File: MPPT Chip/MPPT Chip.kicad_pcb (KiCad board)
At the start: 2 copper layers, 2 parts

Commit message: 11/10 meeting updates
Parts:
- removed REF**: MAX20801, MAX20801:MAX20801
- removed REF**: PinHeader, MAX20801:PinHeader
- added J1: Conn_02x05_Counter_Clockwise, MAX20801:PinHeader, B.Cu at (75.5, 98.3)
- added U0: MAX20801, MAX20801:MAX20801, F.Cu at (79.0, 96.5)
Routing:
- net (no net): track 132.3 -> 0.00 mm, vias 10 -> 0
- net GND: track 0.00 -> 37.9 mm, vias 0 -> 3
- net Net-(J1-Pad5): track 0.00 -> 30.1 mm, vias 0 -> 1
- net Net-(J1-Pad10): track 0.00 -> 26.4 mm, vias 0 -> 1
- net Net-(J1-Pad9): track 0.00 -> 22.1 mm, vias 0 -> 1
- net Net-(J1-Pad1): track 0.00 -> 20.9 mm, vias 0 -> 1
- net Net-(J1-Pad8): track 0.00 -> 17.5 mm, vias 0 -> 1
- net Net-(J1-Pad2): track 0.00 -> 16.3 mm, vias 0 -> 1
- net Net-(J1-Pad6): track 0.00 -> 5.34 mm, vias 0 -> 1
- added copper zone on B.Cu, net GND
- added copper zone on F.Cu, net GND
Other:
- board outline added: 30 x 15 mm

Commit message: gerber files
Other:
- board text added: "BSE MAX 20801"
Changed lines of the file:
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@@
   (general
     (thickness 1.6)
-    (drawings 4)
+    (drawings 5)
     (tracks 84)
     (zones 0)
@@
     (pcbplotparams
       (layerselection 0x010fc_ffffffff)
-      (usegerberextensions false)
+      (usegerberextensions true)
       (usegerberattributes true)
       (usegerberadvancedattributes true)
@@
       (psa4output false)
       (plotreference true)
-      (plotvalue true)
+      (plotvalue false)
       (plotinvisibletext false)
       (padsonsilk false)
@@
       (outputformat 1)
       (mirror false)
-      (drillshape 1)
+      (drillshape 0)
       (scaleselection 1)
-      (outputdirectory ""))
+      (outputdirectory "gerbers/"))
   )
   (net 0 "")
@@
       (net 6 "Net-(J1-Pad5)"))
   )
+  (gr_text "BSE MAX 20801" (at 83.5 103.5) (layer F.SilkS)
+    (effects (font (size 1 1) (thickness 0.15)))
+  )
   (gr_line (start 60 90) (end 60 105) (layer Edge.Cuts) (width 0.001))

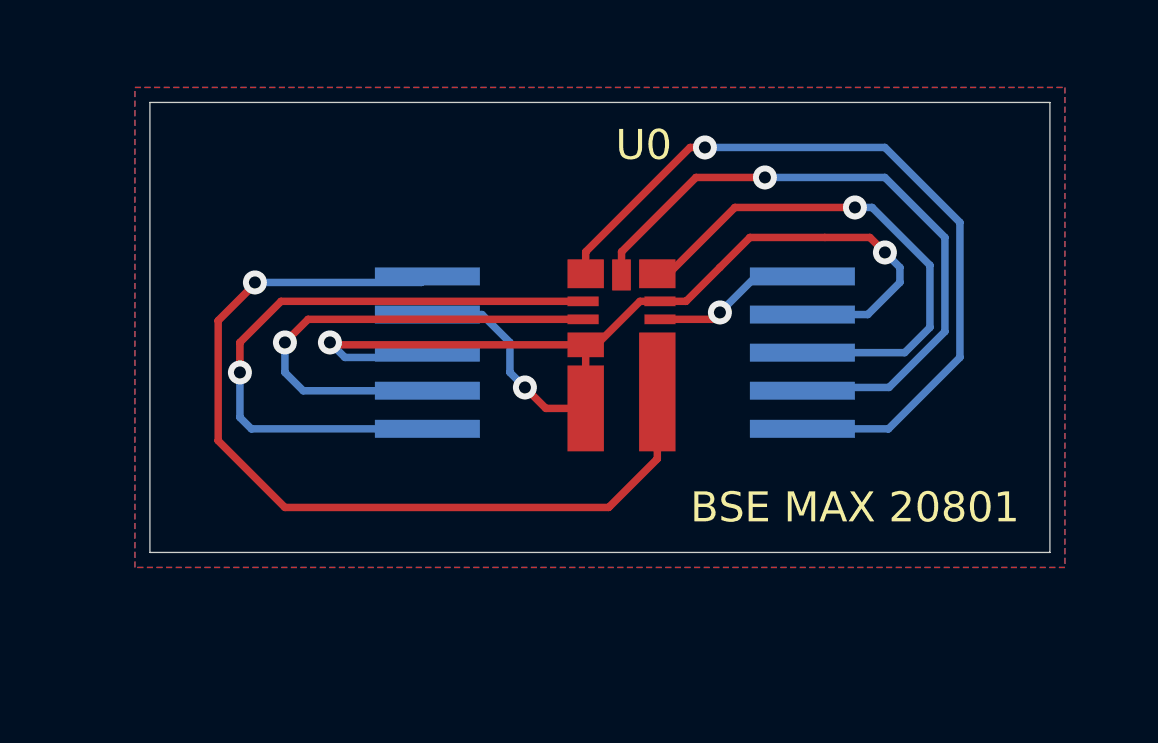
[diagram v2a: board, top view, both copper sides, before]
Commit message: v2 fix based off of durfee review
messed up connections, tried to fix
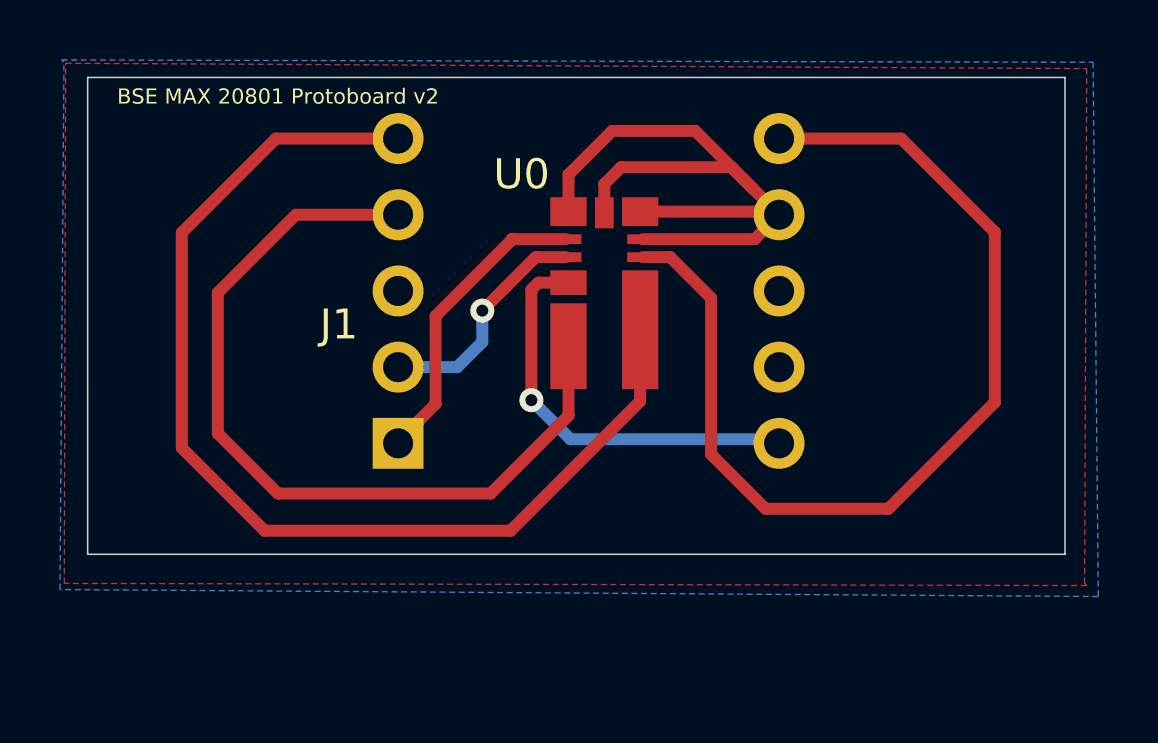
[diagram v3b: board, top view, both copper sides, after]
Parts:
- J1: footprint MAX20801:PinHeader -> Connector_PinHeader_2.54mm:BSE_Connector; moved to F.Cu
- moved J1 10.2 mm to (68.3, 91.2)
- moved U0 2.15 mm to (78.4, 94.4)
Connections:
- net Net-(J1-Pad1) renamed /VCC
- net Net-(J1-Pad5) renamed /OUT
- net Net-(J1-Pad6) renamed /VBST
- J1 pad 10: Net-(J1-Pad10) -> /GND
- J1 pad 2: Net-(J1-Pad2) -> /GND
- J1 pad 3: GND -> /GND
- J1 pad 4: GND -> /PV+
- J1 pad 7: GND -> /GND
- J1 pad 8: Net-(J1-Pad8) -> /GND
- J1 pad 9: Net-(J1-Pad9) -> /GND
- U0 pad 10: Net-(J1-Pad10) -> /GND
- U0 pad 2: Net-(J1-Pad2) -> /GND
- U0 pad 3: GND -> /GND
- U0 pad 4: GND -> /PV+
- U0 pad 7: GND -> /GND
- U0 pad 8: Net-(J1-Pad8) -> /GND
- U0 pad 9: Net-(J1-Pad9) -> /GND
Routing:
- net /GND: track 0.00 -> 48.9 mm, vias 0 -> 2
- net GND: track 37.9 -> 0.00 mm, vias 3 -> 0
- net /VBST: track 5.34 -> 34.5 mm, vias 1 -> 0
- net /PV+: track 0.00 -> 27.7 mm
- net Net-(J1-Pad10): track 26.4 -> 0.00 mm, vias 1 -> 0
- net Net-(J1-Pad9): track 22.1 -> 0.00 mm, vias 1 -> 0
- net Net-(J1-Pad8): track 17.5 -> 0.00 mm, vias 1 -> 0
- net Net-(J1-Pad2): track 16.3 -> 0.00 mm, vias 1 -> 0
- net /VCC: track 20.9 -> 10.2 mm, vias 1 -> 0
- net /OUT: track 30.1 -> 36.3 mm, vias 1 -> 0
- added copper zone on B.Cu, net /GND
- added copper zone on F.Cu, net /GND
- removed copper zone on B.Cu, net GND
- removed copper zone on F.Cu, net GND
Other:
- board size 30 x 15 mm -> 32.6 x 15.9 mm
- board text added: "BSE MAX 20801 Protoboard v2"
- board text removed: "BSE MAX 20801"
